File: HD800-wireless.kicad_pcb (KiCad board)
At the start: 4 copper layers, 72 x 20 mm, 119 parts, among them J1 USB4105-GF-A, J2 Conn_01x03_Pin, J5 TC2050, U1 nRF5340-QKAA, U2 CS43131-CNZR / L mono, U3 CS43131-CNZR / L mono, U4 ETA6003Q3Q, U5 SC7A20, U6 TLV62568DBVR, U7 RT9080, Y1 32MHz / CL=8pF / 10ppm

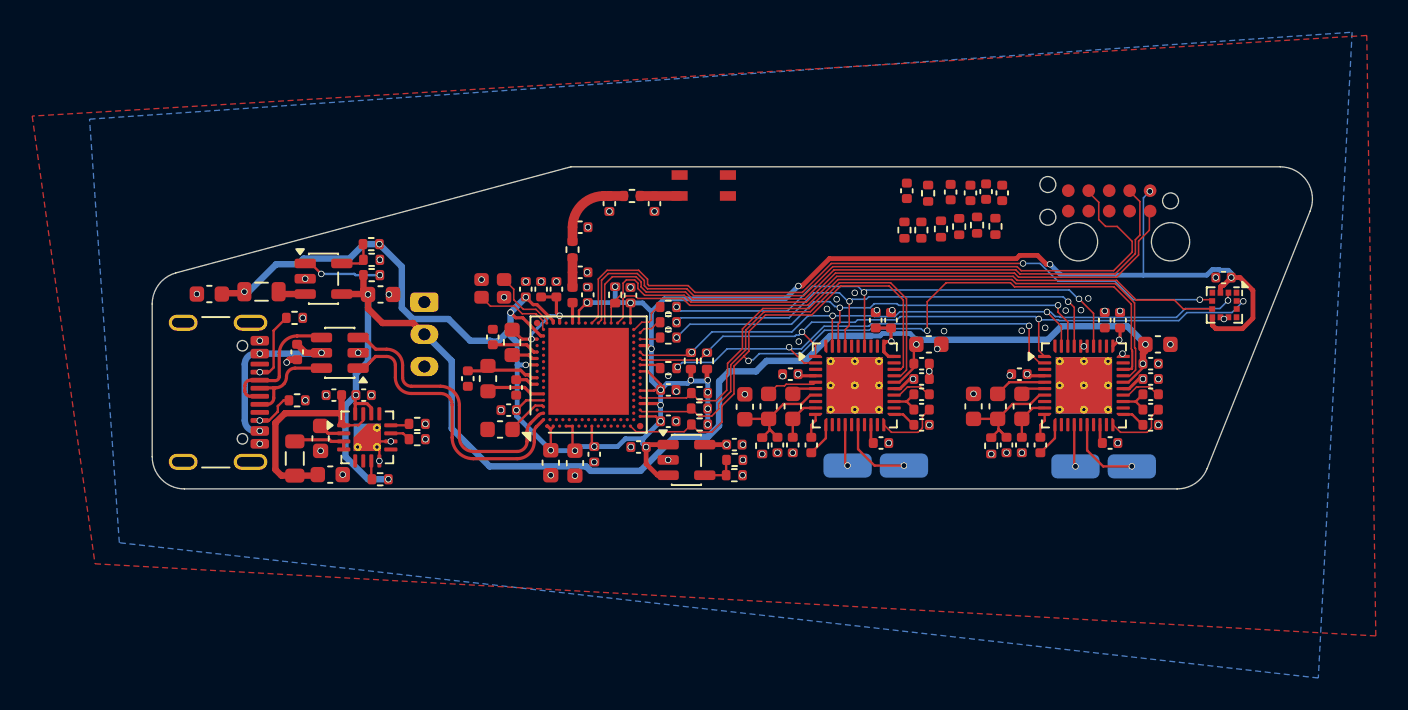
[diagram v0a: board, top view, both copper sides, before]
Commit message: removed firmware
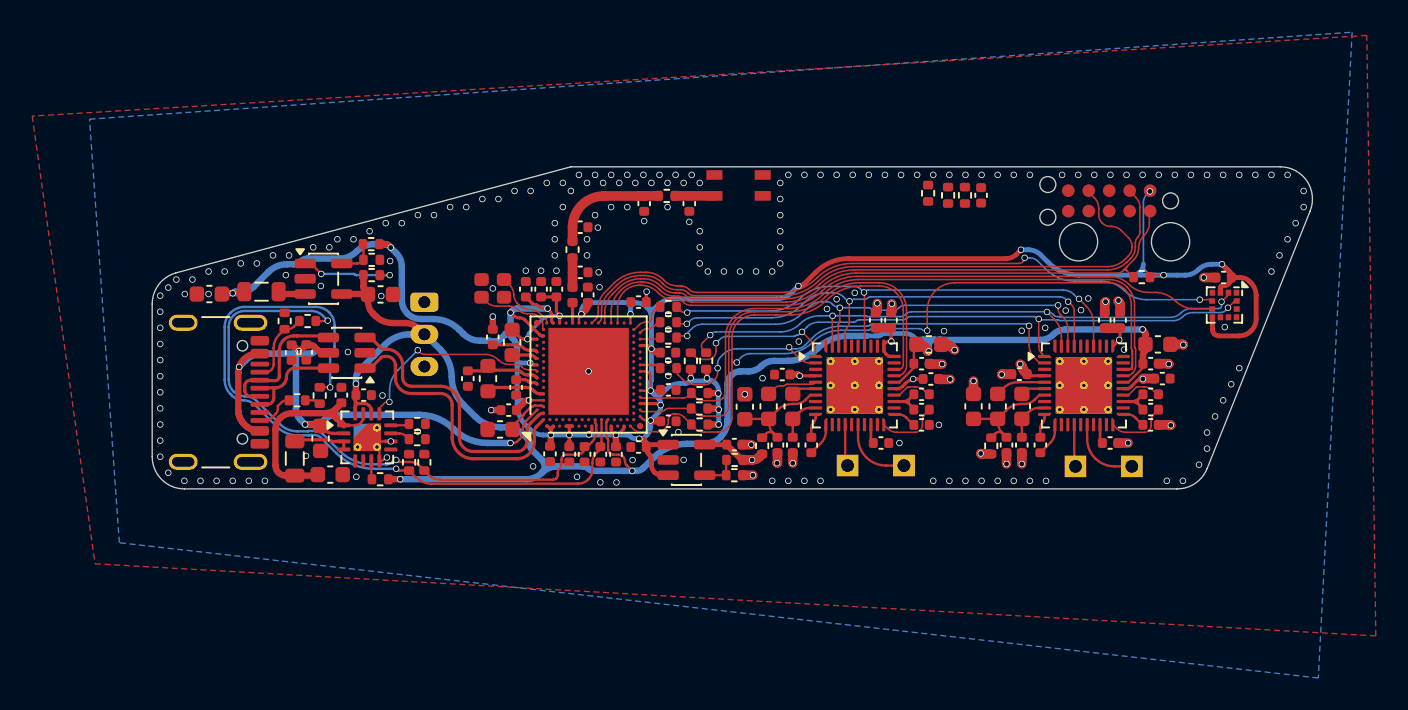
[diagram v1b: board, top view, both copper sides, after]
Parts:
- C37, C40: footprint Capacitor_SMD:C_0603_1608Metric -> Capacitor_SMD:C_0402_1005Metric
- L1: value 2.2uH DFE201210U-1R0M=P2 -> DFE201210U-1R0M
- R1, R4: value 5.1k 1% -> 5.1k
- R10: value R -> 0R
- R13: value 200k 1% -> 200k
- R14, R2, R21, R3, R5, R6: value 100k 1% -> 100k
- R20: value 330k 1% -> 330k
- R36, R37: value 2R 1% -> 2R
- TP1, TP2, TP3, TP4: footprint Connector_Wire:SolderWirePad_1x01_SMD_1.5x3mm -> Connector_PinHeader_2.00mm:PinHeader_1x01_P2.00mm_Vertical
- moved C3 44.3 mm to (173.6, 54.5), turned to -90 degrees
- moved R5 43.3 mm to (174.4, 57.2)
- moved R2 40.9 mm to (173.7, 52.6), turned to 180 degrees
- moved R3 37.3 mm to (180.9, 61.4)
- moved R6 36.1 mm to (179.9, 61.4)
- moved R23 32.7 mm to (225.4, 49.9), turned to 180 degrees
- moved C2 28.1 mm to (191.8, 60.9), turned to -90 degrees
- moved C1 28.0 mm to (190.8, 60.9), turned to -90 degrees
- moved C33 17.9 mm to (196.0, 54.5), turned to 0 degrees
- moved R20 3.47 mm to (214.5, 44.8)
- moved R21 3.47 mm to (213.4, 44.8), turned to -90 degrees
- moved C10 2.16 mm to (194.6, 45.3)
- moved AE1 2.16 mm to (200.4, 43.2)
- moved C12 2.16 mm to (197.3, 45.3)
- moved R10 2.16 mm to (195.9, 44.8)
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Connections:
- R1 pad 1: Net-(J1-CC2) -> GND
- R1 pad 2: GND -> Net-(J1-CC2)
- R2 pad 2: CC1 -> Net-(J1-CC1)
- R4 pad 1: Net-(J1-CC1) -> GND
- R4 pad 2: GND -> Net-(J1-CC1)
- R5 pad 1: CC2 -> Net-(J1-CC2)
- U1 pad A17: unconnected-(U1-P1.13-PadA17) -> USB_DET
- U1 pad AB2: VBAT_ADC -> VBAT
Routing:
- net CC2_ADC: track 0.00 -> 45.1 mm, vias 0 -> 2
- net CC1_ADC: track 0.00 -> 38.9 mm, vias 0 -> 2
- net VBUS: track 13.3 -> 38.2 mm, vias 3 -> 4
- net GND: track 3.60 -> 18.5 mm, vias 77 -> 216
- net VDD_nRF: track 140.5 -> 154.9 mm, vias 26 -> 27
- net USB_DET: track 0.00 -> 12.7 mm, vias 0 -> 2
- net VBAT: track 86.7 -> 95.5 mm, vias 6 -> 5
- net VDD_1V8: track 57.7 -> 65.2 mm, vias 10 -> 8
- net I2C_SDA: track 43.2 -> 39.1 mm
- net I2C_SCL: track 43.9 -> 40.4 mm
- net SWDCLK: track 43.1 -> 40.8 mm
- net Net-(C10-Pad1): track 5.09 -> 7.25 mm
- net SWDIO: track 41.7 -> 39.7 mm
- net /03 MCU RF/ACC_INT1: track 43.6 -> 41.9 mm
- net DAC_RESET: track 62.8 -> 64.2 mm
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
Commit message: ??
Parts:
- added R11: 100k, Resistor_SMD:R_0402_1005Metric, F.Cu at (193.7, 61.8)
- added R17: 510k, Resistor_SMD:R_0402_1005Metric, F.Cu at (194.6, 61.8)
- R2, R5: value 100k -> 510k
- R25, R26, R27, R28: value 4.7k -> 10k
- moved C35 10.9 mm to (188.7, 60.8), turned to -90 degrees
- moved C34 6.57 mm to (189.8, 60.8), turned to -90 degrees
- moved C40 6.41 mm to (185.9, 55.8), turned to 180 degrees
- moved C31 5.66 mm to (185.9, 52.5)
- moved C37 3.50 mm to (186.0, 58.6), turned to 180 degrees
- moved C25 2.43 mm to (185.9, 56.8), turned to 180 degrees
- moved L4 1.55 mm to (184.3, 57.6)
- moved C26 1.51 mm to (185.9, 54.9), turned to 180 degrees
- moved C27 1.19 mm to (185.9, 57.7), turned to 180 degrees
- moved L3 0.98 mm to (185.4, 53.6), turned to 0 degrees
- moved R25 0.95 mm to (198.4, 55.0)
- moved R26 0.95 mm to (197.4, 55.0)
- moved C36 0.95 mm to (196.1, 57.8)
- moved C28 0.58 mm to (185.4, 59.9)
- moved R32 0.45 mm to (196.1, 56.0)
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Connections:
- R24 pad 2: VDD_nRF -> VDD_1V8
- R25 pad 2: VDD_nRF -> VDD_1V8
- R26 pad 2: VDD_nRF -> VDD_1V8
- R27 pad 2: VDD_nRF -> VDD_1V8
- R28 pad 2: VDD_nRF -> VDD_1V8
- U1 pad AB2: VBAT -> VBAT_ADC
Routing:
- net VDD_nRF: track 154.9 -> 141.5 mm, vias 27 -> 22
- net VDD_1V8: track 65.2 -> 76.3 mm, vias 8 -> 13
- net VBAT_ADC: track 0.00 -> 4.66 mm
- net VBAT: track 95.5 -> 91.1 mm
- net I2C_SDA: track 39.1 -> 42.9 mm
- net Net-(U1-DCC): track 1.62 -> 4.31 mm
- net I2C_SCL: track 40.4 -> 43.0 mm
- net GND: track 18.5 -> 16.5 mm, vias 216 -> 226
- net Net-(U1-DECN): track 2.87 -> 1.41 mm
- net Net-(U1-DCCD): track 3.32 -> 4.63 mm
- net D_N: track 25.6 -> 26.8 mm
- net D_P: track 23.0 -> 24.1 mm
- net USB_DET: track 12.7 -> 13.8 mm
- net VBUS: track 38.2 -> 39.1 mm
- net DAC_RESET: track 64.2 -> 63.5 mm
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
